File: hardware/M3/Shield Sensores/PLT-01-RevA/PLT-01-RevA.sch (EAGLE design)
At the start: 5 parts

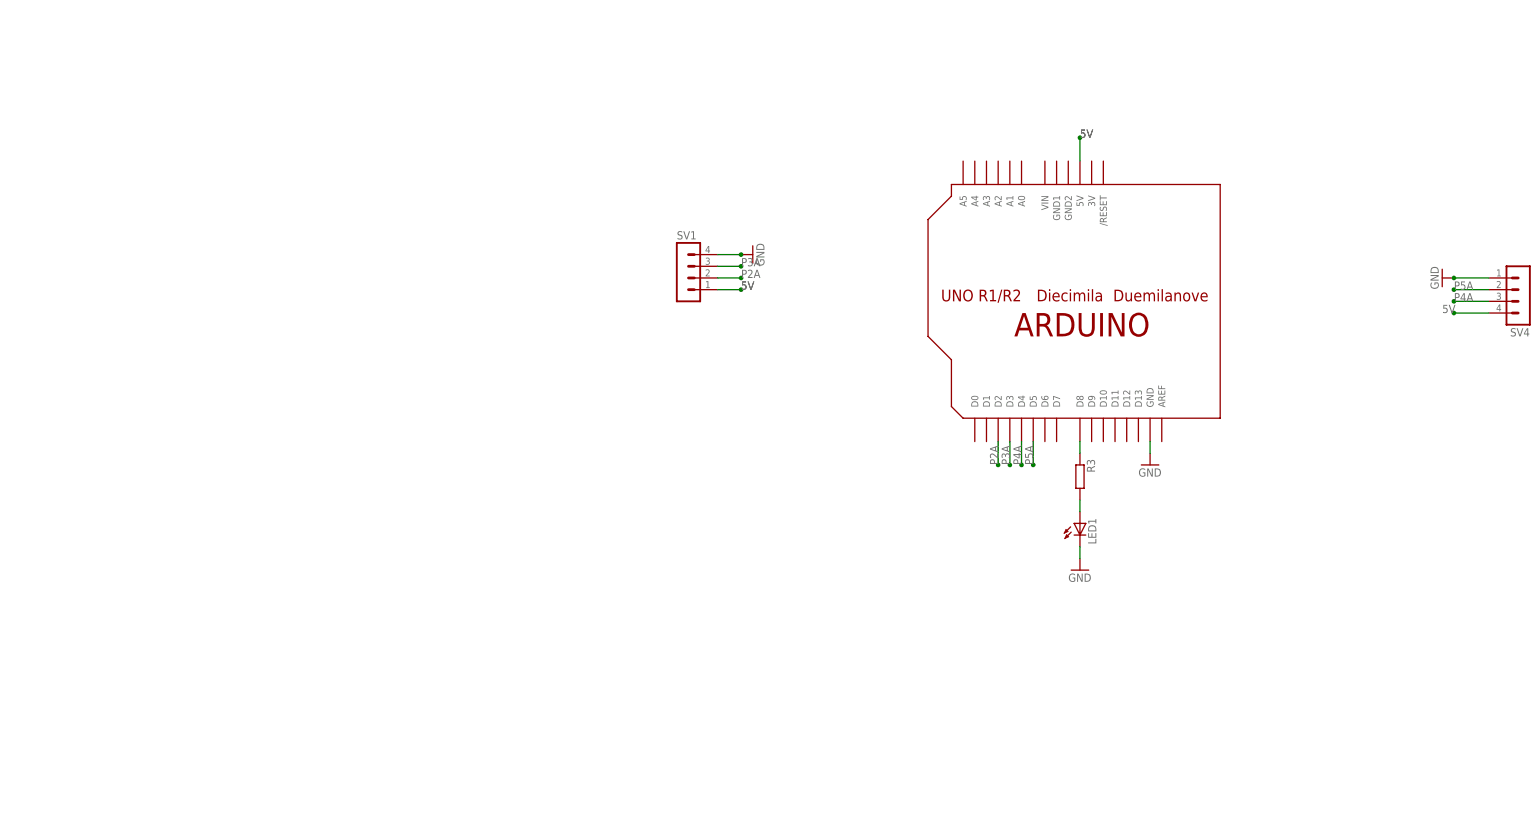
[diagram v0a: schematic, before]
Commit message: Archivos a png
paso archivos de cnc a png para que se puedan ver los cortes sin tener que descargar aplicaciones
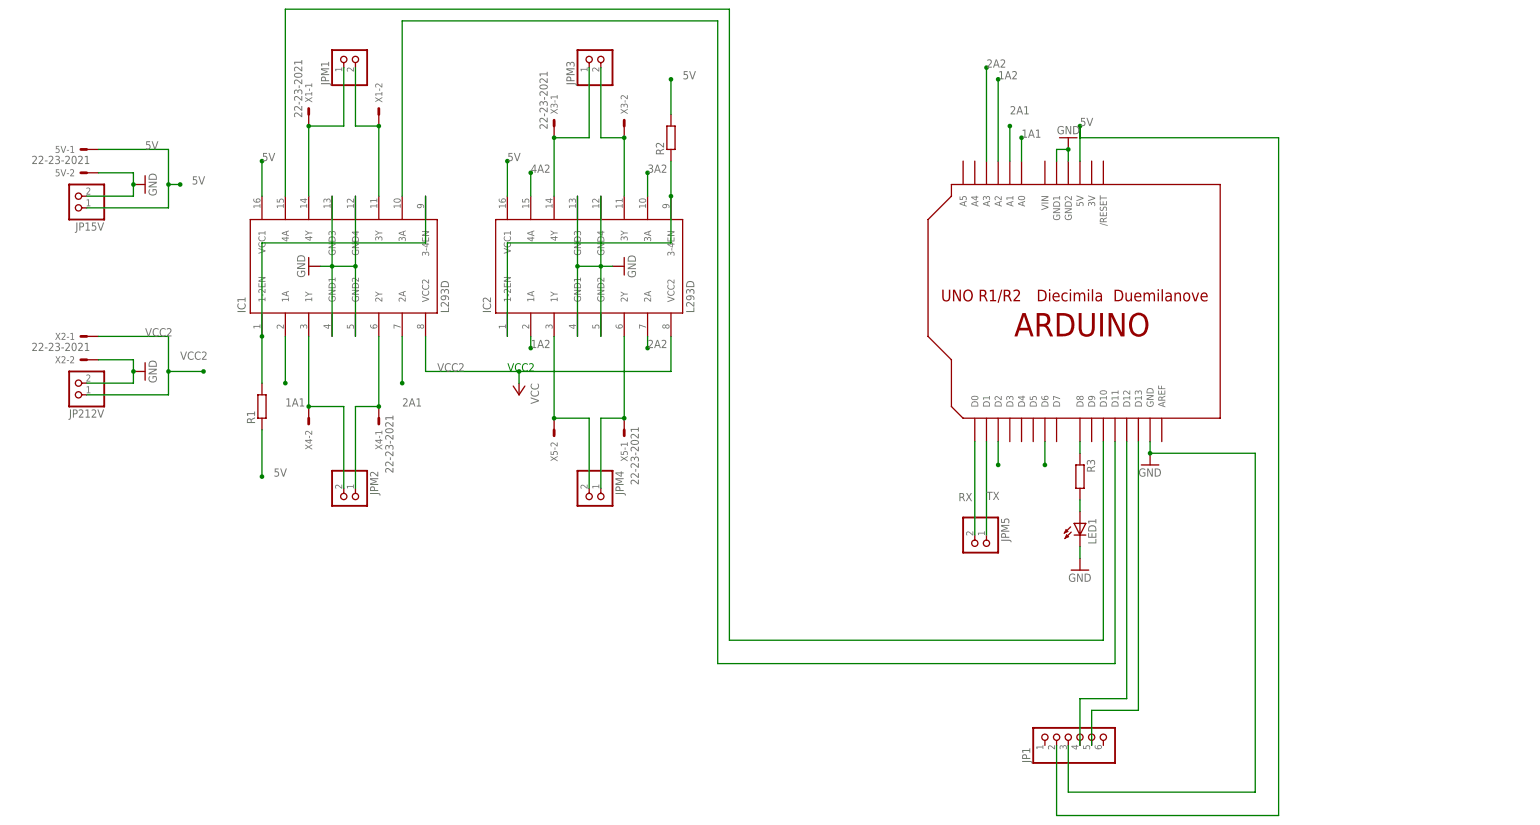
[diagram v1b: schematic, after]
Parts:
- removed SV1, SV4: (no value), con-lstb:MA04-1
- added 5V, X1, X2, X3, X4, X5: 22-23-2021, con-molex:22-23-2021
- added IC1, IC2: L293D, st-microelectronics:L293D
- added JP1: (no value), pinhead:PINHD-1X6
- added JP15V, JP212V, JPM1, JPM2, JPM3, JPM4, JPM5: (no value), pinhead:PINHD-1X2
- added R1, R2: (no value), resistor:R-EU_0207/10
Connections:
- removed net P2A: SV1.2, U$1.D2
- removed net P3A: SV1.3, U$1.D3
- removed net P4A: SV4.3, U$1.D4
- removed net P5A: SV4.2, U$1.D5
- new net 1A1: IC1.1A, U$1.A0
- new net 1A2: IC2.1A, U$1.A2
- new net 2A1: IC1.2A, U$1.A1
- new net 2A2: IC2.2A, U$1.A3
- new net 3A2: IC2.3A, U$1.D2
- new net 4A2: IC2.4A, U$1.D6
- new net N$1: IC1.1Y, JPM2.2, X4-2.S
- new net N$11: IC1.3A, U$1.D11
- new net N$13: JP1.4, U$1.D12
- new net N$14: IC1.1-2EN, IC1.3-4EN, R1.2
- new net N$19: JP1.5, U$1.D13
- new net N$2: IC1.2Y, JPM2.1, X4-1.S
- new net N$22: IC1.4A, U$1.D10
- new net N$3: IC2.1Y, JPM4.2, X5-2.S
- new net N$4: IC2.2Y, JPM4.1, X5-1.S
- new net N$5: IC2.4Y, JPM3.1, X3-1.S
- new net N$6: IC2.3Y, JPM3.2, X3-2.S
- new net N$7: IC1.4Y, JPM1.1, X1-1.S
- new net N$8: IC1.3Y, JPM1.2, X1-2.S
- new net N$9: IC2.1-2EN, IC2.3-4EN, R2.1
- new net RX: JPM5.2, U$1.D0
- new net TX: JPM5.1, U$1.D1
- new net VCC2: IC1.VCC2, IC2.VCC2, JP212V.1, X2-1.S
- net 5V: now also 5V-1.S, IC1.VCC1, IC2.VCC1, JP1.2, JP15V.1, R1.1, R2.2; no longer SV1.1, SV4.4
- net GND: now also 5V-2.S, IC1.GND1, IC1.GND2, IC1.GND3, IC1.GND4, IC2.GND1, IC2.GND2, IC2.GND3, IC2.GND4, JP1.3, JP15V.2, JP212V.2, U$1.GND1, U$1.GND2, X2-2.S; no longer SV1.4, SV4.1
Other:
- note added: "VCC2"

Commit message: Actualizaciones
cambios en placa 2
cambio de ubicacion de la carpeta vehiculo
agregamos archivos svg y redimensionados
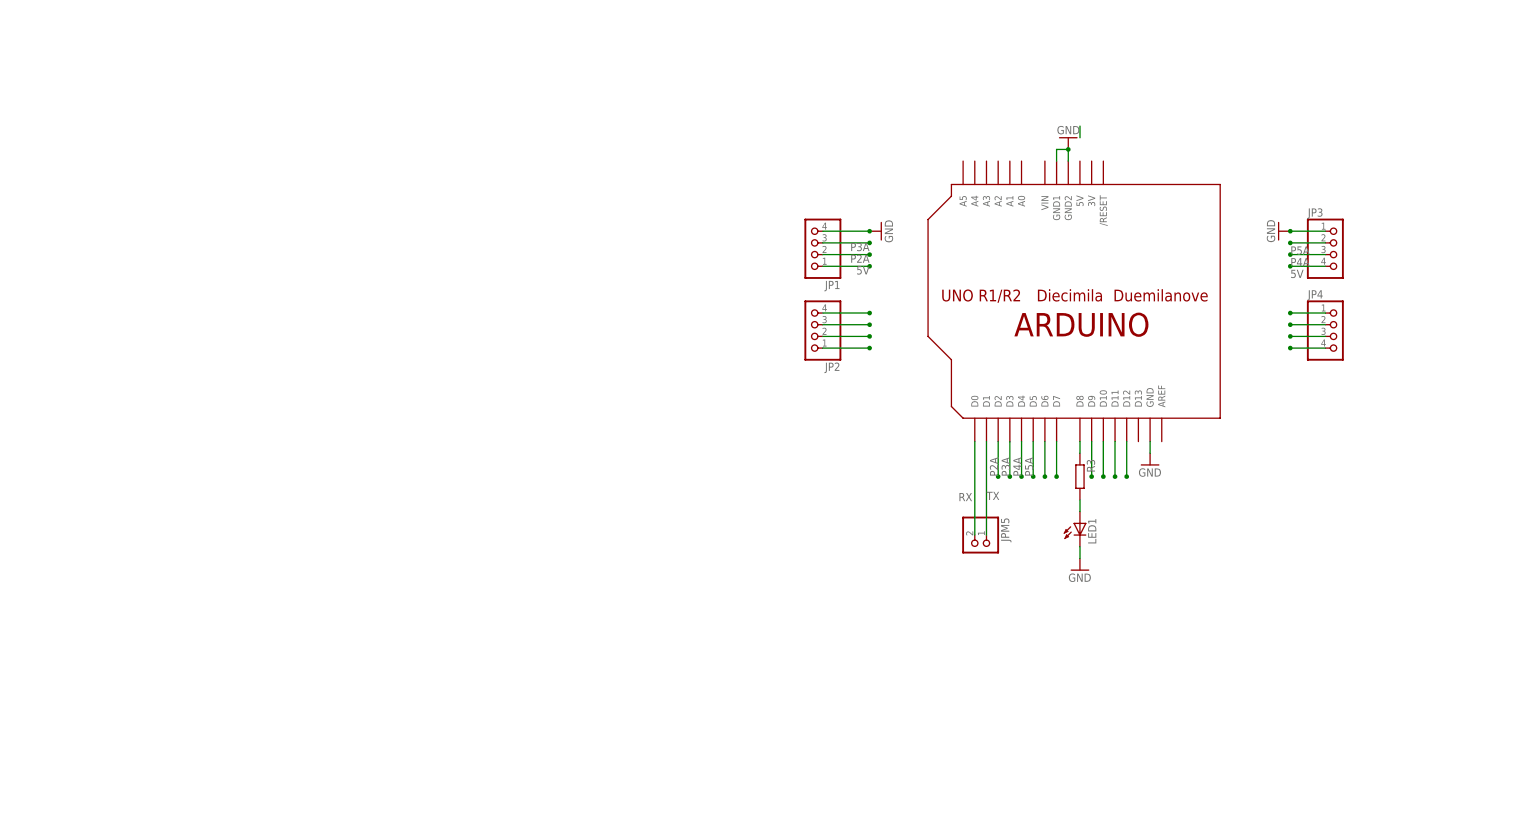
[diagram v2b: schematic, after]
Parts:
- removed 5V, X1, X2, X3, X4, X5: 22-23-2021, con-molex:22-23-2021
- removed IC1, IC2: L293D, st-microelectronics:L293D
- removed JP15V, JP212V, JPM1, JPM2, JPM3, JPM4: (no value), pinhead:PINHD-1X2
- removed R1, R2: (no value), resistor:R-EU_0207/10
- added JP2, JP3, JP4: (no value), pinhead:PINHD-1X4
- JP1: device pinhead:PINHD-1X6 -> pinhead:PINHD-1X4
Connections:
- removed net 1A1: IC1.1A, U$1.A0
- removed net 1A2: IC2.1A, U$1.A2
- removed net 2A1: IC1.2A, U$1.A1
- removed net 2A2: IC2.2A, U$1.A3
- removed net 3A2: IC2.3A, U$1.D2
- removed net 4A2: IC2.4A, U$1.D6
- removed net N$1: IC1.1Y, JPM2.2, X4-2.S
- removed net N$11: IC1.3A, U$1.D11
- removed net N$13: JP1.4, U$1.D12
- removed net N$2: IC1.2Y, JPM2.1, X4-1.S
- removed net N$22: IC1.4A, U$1.D10
- removed net N$3: IC2.1Y, JPM4.2, X5-2.S
- removed net N$6: IC2.3Y, JPM3.2, X3-2.S
- removed net N$7: IC1.4Y, JPM1.1, X1-1.S
- removed net VCC2: IC1.VCC2, IC2.VCC2, JP212V.1, X2-1.S
- new net N$15: JP2.1
- new net N$17: JP4.2
- new net N$30: U$1.D7
- new net N$31: U$1.D10
- new net N$32: U$1.D12
- new net N$35: U$1.D6
- new net N$36: U$1.D9
- new net N$37: U$1.D11
- new net P2A: JP1.2, U$1.D2
- new net P3A: JP1.3, U$1.D3
- new net P4A: JP3.3, U$1.D4
- new net P5A: JP3.2, U$1.D5
- net 5V: now also JP1.1, JP3.4; no longer 5V-1.S, IC1.VCC1, IC2.VCC1, JP1.2, JP15V.1, R1.1, R2.2, U$1.5V
- net GND: now also JP1.4, JP3.1; no longer 5V-2.S, IC1.GND1, IC1.GND2, IC1.GND3, IC1.GND4, IC2.GND1, IC2.GND2, IC2.GND3, IC2.GND4, JP1.3, JP15V.2, JP212V.2, X2-2.S
- net N$14: now also JP2.3; no longer IC1.1-2EN, IC1.3-4EN, R1.2
- net N$19: now also JP4.4; no longer JP1.5, U$1.D13
- net N$4: now also JP2.4; no longer IC2.2Y, JPM4.1, X5-1.S
- net N$5: now also JP2.2; no longer IC2.4Y, JPM3.1, X3-1.S
- net N$8: now also JP4.1; no longer IC1.3Y, JPM1.2, X1-2.S
- net N$9: now also JP4.3; no longer IC2.1-2EN, IC2.3-4EN, R2.1
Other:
- note removed: "VCC2"
